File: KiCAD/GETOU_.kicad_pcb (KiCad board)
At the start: 2 copper layers, 106.5 x 58 mm, 25 parts, among them U1 XIAO-RP2040-DIP

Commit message: Add and modify files
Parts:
- moved U1 12.8 mm to (191.0, 93.5)
- moved S12 11.7 mm to (170.5, 110.5)
- moved S11 11.2 mm to (170.8, 92.0)
- moved S9 10.8 mm to (152.3, 110.5)
- moved S10 10.5 mm to (170.8, 73.4)
- moved S8 9.95 mm to (152.3, 92.0)
- moved S6 9.55 mm to (133.5, 110.5)
- moved S7 9.18 mm to (152.3, 73.4)
- moved S3 8.63 mm to (115.0, 110.5)
- moved D10 8.57 mm to (96.0, 106.7)
- moved D5 8.57 mm to (96.0, 88.9)
- moved D1 8.57 mm to (96.0, 74.7)
- moved D11 8.57 mm to (96.0, 110.2)
- moved D12 8.57 mm to (96.0, 113.8)
- moved D2 8.57 mm to (96.0, 78.2)
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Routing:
- net Net-(D11-A): track 96.5 -> 114.3 mm
- net row0: track 120.5 -> 130.7 mm
- net col3: track 106.2 -> 114.2 mm
- net col1: track 124.5 -> 131.3 mm
- net Net-(D4-A): track 42.4 -> 49.0 mm
- net Net-(D6-A): track 42.9 -> 49.0 mm
- net col2: track 117.8 -> 123.4 mm
- net col0: track 149.0 -> 143.5 mm
- net row2: track 73.6 -> 78.0 mm
- net row1: track 98.8 -> 103.2 mm
- net Net-(D8-A): track 53.7 -> 56.5 mm
- net Net-(D9-A): track 67.8 -> 70.4 mm, vias 1 -> 0
- net Net-(D3-A): track 42.4 -> 44.9 mm
- net Net-(D2-A): track 30.4 -> 28.0 mm
- net Net-(D12-A): track 52.5 -> 54.7 mm
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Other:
- board size 106.5 x 58 mm -> 111.5 x 62 mm

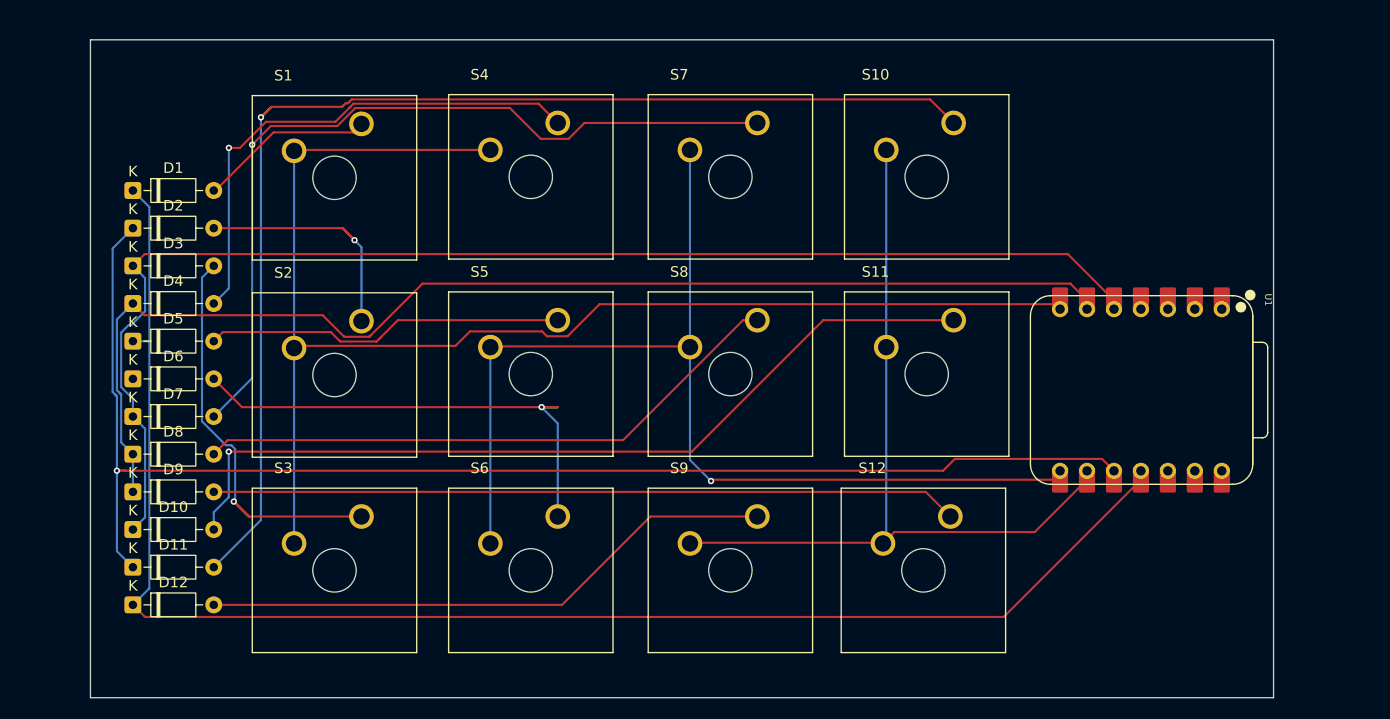
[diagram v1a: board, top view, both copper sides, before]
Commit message: Deleted files:     Firmware/qmk/keyboards/getou_/config.h     Firmware/qmk/keyboards/getou_/rules.mk     Fusion/PCB.stl
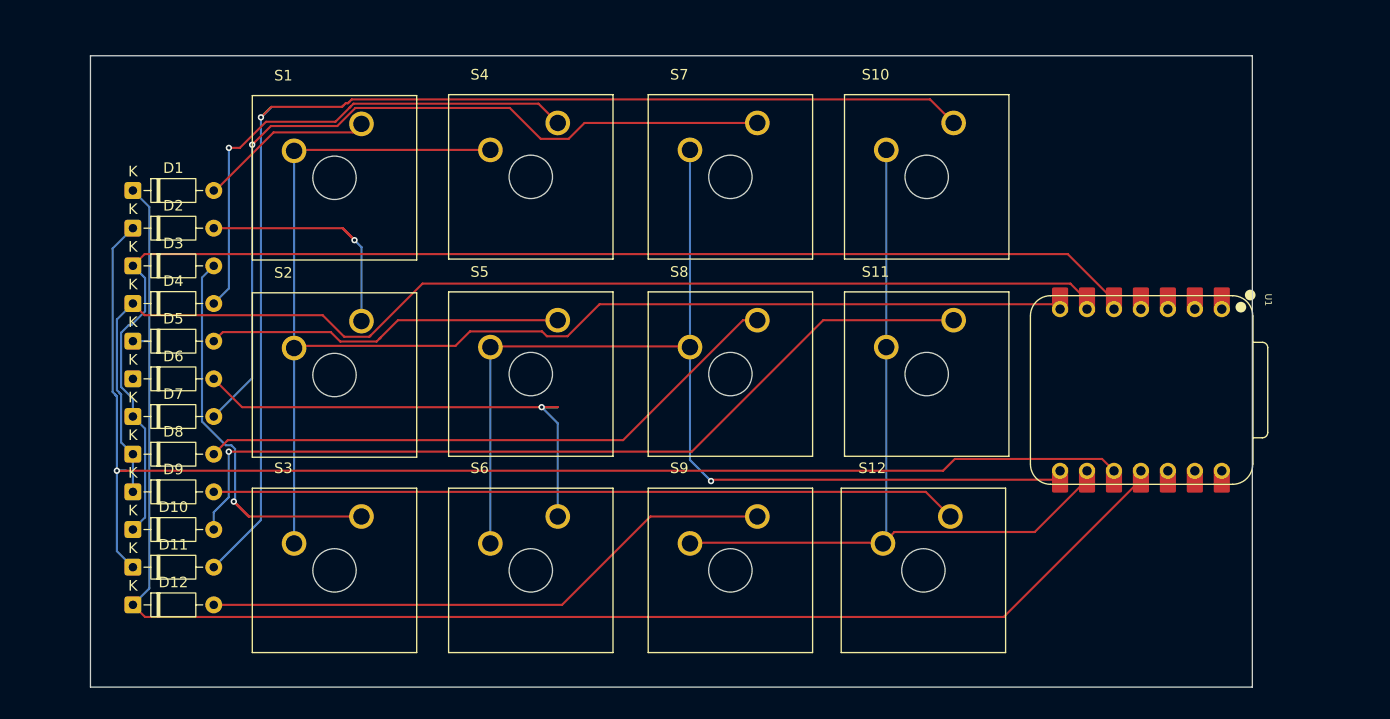
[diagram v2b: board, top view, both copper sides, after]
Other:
- board size 111.5 x 62 mm -> 109.5 x 59.5 mm
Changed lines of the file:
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@@
 		)
 	)
-	(gr_line
-		(start 203.5 93)
-		(end 203.5 60.5)
+	(gr_rect
+		(start 92 62)
+		(end 201.5 121.5)
 		(stroke
 			(width 0.05)
 			(type default)
 		)
-		(layer "Edge.Cuts")
-	)
-	(gr_line
-		(start 203.5 60.5)
-		(end 92 60.5)
-		(stroke
-			(width 0.05)
-			(type default)
-		)
-		(layer "Edge.Cuts")
-	)
-	(gr_line
-		(start 92 60.5)
-		(end 92 122.5)
-		(stroke
-			(width 0.05)
-			(type default)
-		)
-		(layer "Edge.Cuts")
-	)
-	(gr_line
-		(start 203.5 122.5)
-		(end 203.5 93)
-		(stroke
-			(width 0.05)
-			(type default)
-		)
-		(layer "Edge.Cuts")
-	)
-	(gr_line
-		(start 92 122.5)
-		(end 203.5 122.5)
-		(stroke
-			(width 0.05)
-			(type default)
-		)
+		(fill no)
 		(layer "Edge.Cuts")
 	)
@@
 		(polygon
 			(pts
-				(xy 203.5 60.5) (xy 203.5 122.5) (xy 92 122.5) (xy 92 60.5)
+				(xy 201.5 62) (xy 201.5 121.5) (xy 92 121.5) (xy 92 62)
 			)
 		)

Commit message: Add stuff
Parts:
- moved U1 8.82 mm to (199.6, 91.6), turned to 0 degrees
- moved S10 7.14 mm to (177.8, 72.0)
- moved S11 7.07 mm to (177.8, 91.0)
- moved S12 7.02 mm to (177.5, 110.0)
- moved S7 6.84 mm to (159.0, 72.0)
- moved S8 6.76 mm to (159.0, 91.0)
- moved S9 6.71 mm to (159.0, 110.0)
- moved S1 6.61 mm to (121.3, 71.5)
- moved S4 6.35 mm to (139.6, 71.5)
- moved S2 6.10 mm to (121.0, 91.0)
- moved S5 6.08 mm to (139.5, 91.0)
- moved S3 6.02 mm to (121.0, 110.0)
- moved S6 6.02 mm to (139.5, 110.0)
- moved D1 5.18 mm to (97.7, 69.8)
- moved D10 5.18 mm to (97.7, 101.8)
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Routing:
- net col0: track 143.5 -> 0.00 mm
- net col1: track 131.3 -> 0.00 mm, vias 1 -> 0
- net row0: track 130.7 -> 0.00 mm
- net col2: track 123.4 -> 0.00 mm
- net Net-(D11-A): track 114.3 -> 0.00 mm, vias 1 -> 0
- net col3: track 114.2 -> 0.00 mm
- net row1: track 103.2 -> 0.00 mm, vias 1 -> 0
- net Net-(D10-A): track 81.4 -> 0.00 mm, vias 1 -> 0
- net Net-(D7-A): track 79.3 -> 0.00 mm, vias 1 -> 0
- net row2: track 78.0 -> 0.00 mm
- net Net-(D9-A): track 70.4 -> 0.00 mm
- net Net-(D8-A): track 56.5 -> 0.00 mm
- net Net-(D12-A): track 54.7 -> 0.00 mm
- net Net-(D6-A): track 49.0 -> 0.00 mm, vias 1 -> 0
- net Net-(D4-A): track 49.0 -> 0.00 mm, vias 1 -> 0
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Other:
- board outline removed

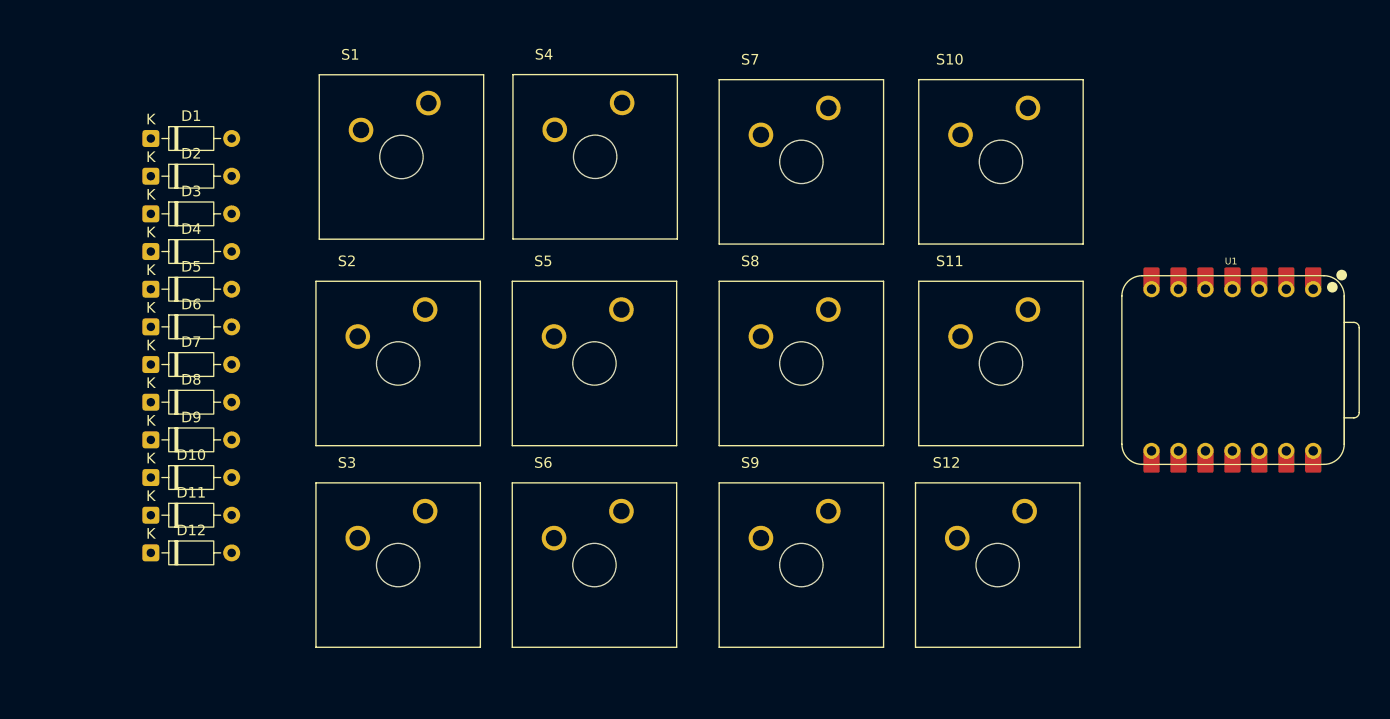
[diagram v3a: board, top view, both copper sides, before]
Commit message: Fix values in GETOU_ project files for improved accuracy
- Updated numerical values in GETOU_.kicad_prl to correct component specifications.
- Adjusted positions of global labels in GETOU_.kicad_sch for better alignment and clarity.
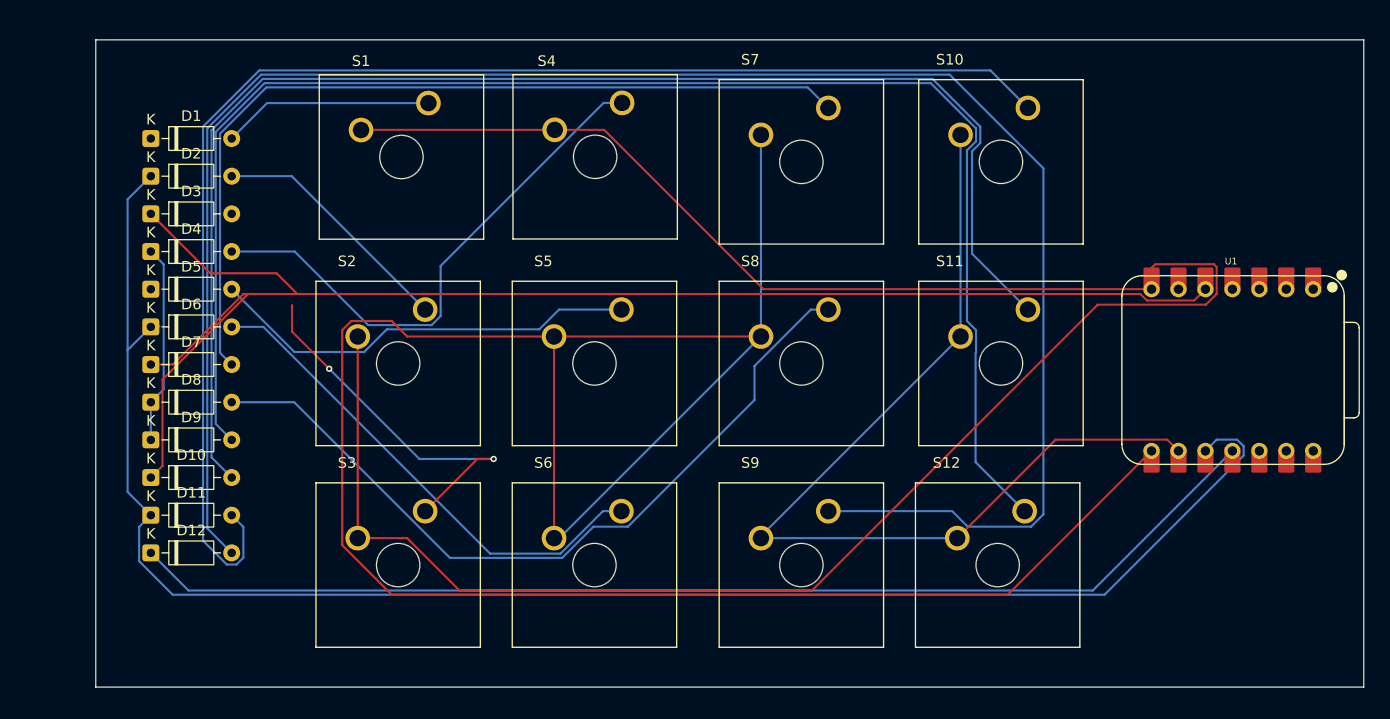
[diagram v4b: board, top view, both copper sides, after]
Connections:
- D6 pad 1: unconnected-(D6-K-Pad1) -> col1
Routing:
- net row1: track 0.00 -> 209.9 mm
- net row0: track 0.00 -> 205.2 mm
- net Net-(D12-A): track 0.00 -> 179.5 mm
- net col1: track 0.00 -> 159.4 mm
- net Net-(D9-A): track 0.00 -> 143.7 mm
- net col2: track 0.00 -> 143.5 mm
- net Net-(D11-A): track 0.00 -> 129.9 mm
- net Net-(D10-A): track 0.00 -> 129.6 mm
- net col0: track 0.00 -> 108.8 mm
- net row2: track 0.00 -> 89.4 mm
- net Net-(D7-A): track 0.00 -> 82.2 mm
- net Net-(D8-A): track 0.00 -> 73.9 mm
- net Net-(D4-A): track 0.00 -> 51.1 mm
- net Net-(D6-A): track 0.00 -> 47.2 mm
- net Net-(D5-A): track 0.00 -> 40.8 mm
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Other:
- board outline added: 119.5 x 61 mm

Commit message: Modify Files
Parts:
- moved S5 2.60 mm to (142.1, 90.6)
- moved S6 2.57 mm to (142.1, 110.0)
- moved S4 2.53 mm to (142.1, 71.1)
- moved U1 1.95 mm to (200.5, 89.9)
- moved S7 1.68 mm to (160.5, 71.2)
- moved S8 1.52 mm to (160.5, 90.6)
- moved S12 1.50 mm to (179.0, 110.0)
- moved S10 1.46 mm to (179.0, 71.1)
- moved S9 1.46 mm to (160.5, 110.0)
- moved S11 1.27 mm to (179.0, 90.6)
- moved S3 1.09 mm to (122.0, 110.4)
- moved S2 1.00 mm to (122.0, 91.0)
- moved S1 0.69 mm to (122.0, 71.6)
- moved D3 0.21 mm to (97.5, 76.8)
- moved D4 0.21 mm to (97.5, 80.3)
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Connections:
- D10 pad 1: col2 -> col1
- D11 pad 1: col1 -> col0
- D12 pad 1: col0 -> col2
- D4 pad 1: col3 -> col0
- D5 pad 1: col0 -> col1
- D6 pad 1: col1 -> col2
- D7 pad 1: col2 -> col0
- D8 pad 1: col3 -> col1
- D9 pad 1: col3 -> col2
- S10 pad 1: row2 -> row3
- S11 pad 1: row2 -> row3
- S12 pad 1: row2 -> row3
- S4 pad 1: row0 -> row1
- S7 pad 1: row1 -> row2
- S8 pad 1: row1 -> row2
- U1 pad 6: col3 -> row3
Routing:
- net row1: track 209.9 -> 38.9 mm
- net row0: track 205.2 -> 41.4 mm, vias 0 -> 2
- net col1: track 159.4 -> 0.00 mm
- net Net-(D11-A): track 129.9 -> 0.00 mm
- net row3: track 0.00 -> 106.0 mm
- net Net-(D12-A): track 179.5 -> 104.8 mm
- net Net-(D9-A): track 143.7 -> 88.9 mm
- net Net-(D6-A): track 47.2 -> 0.00 mm
- net Net-(D10-A): track 129.6 -> 91.6 mm
- net col0: track 108.8 -> 144.3 mm
- net Net-(D3-A): track 35.5 -> 0.00 mm, vias 2 -> 0
- net Net-(D8-A): track 73.9 -> 109.1 mm
- net col3: track 18.8 -> 0.00 mm
- net col2: track 143.5 -> 160.7 mm, vias 0 -> 1
- net Net-(D7-A): track 82.2 -> 68.6 mm
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
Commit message: Modifiy Files
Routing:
- net col1: track 0.00 -> 134.4 mm, vias 0 -> 1
- net Net-(D8-A): track 109.1 -> 216.7 mm
- net Net-(D11-A): track 0.00 -> 106.5 mm, vias 0 -> 1
- net Net-(D12-A): track 104.8 -> 207.5 mm
- net Net-(D10-A): track 91.6 -> 180.2 mm
- net Net-(D9-A): track 88.9 -> 174.9 mm
- net row0: track 41.4 -> 122.7 mm
- net row3: track 106.0 -> 171.7 mm
- net row1: track 38.9 -> 99.0 mm
- net Net-(D6-A): track 0.00 -> 52.1 mm, vias 0 -> 2
- net col2: track 160.7 -> 206.7 mm
- net row2: track 77.9 -> 121.4 mm
- net Net-(D3-A): track 0.00 -> 42.0 mm, vias 0 -> 1
- net Net-(D7-A): track 68.6 -> 103.3 mm
- net col0: track 144.3 -> 176.5 mm
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
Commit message: Modify Files
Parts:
- moved D12 7.27 mm to (98.0, 116.0)
- moved D11 6.32 mm to (98.0, 111.5)
- moved D10 5.37 mm to (98.0, 107.0)
- moved D9 4.38 mm to (98.0, 102.5)
- moved D8 3.59 mm to (98.0, 98.1)
- moved S5 2.91 mm to (139.3, 91.5)
- moved S4 2.90 mm to (139.3, 72.0)
- moved D1 2.88 mm to (98.2, 66.9)
- moved S6 2.76 mm to (139.3, 110.0)
- moved D7 2.65 mm to (98.0, 93.6)
- moved S8 2.63 mm to (158.0, 91.5)
- moved S7 2.60 mm to (158.0, 72.0)
- moved S9 2.46 mm to (158.0, 110.0)
- moved D2 2.35 mm to (98.2, 71.0)
- moved D6 1.72 mm to (98.0, 89.1)
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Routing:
- net row0: track 122.7 -> 293.5 mm, vias 2 -> 1
- net col1: track 134.4 -> 275.1 mm, vias 1 -> 0
- net col0: track 176.5 -> 308.2 mm
- net row1: track 99.0 -> 223.3 mm
- net Net-(D8-A): track 216.7 -> 103.0 mm
- net Net-(D11-A): track 106.5 -> 207.2 mm
- net Net-(D9-A): track 174.9 -> 79.2 mm
- net row3: track 171.7 -> 86.6 mm
- net Net-(D12-A): track 207.5 -> 126.3 mm
- net col2: track 206.7 -> 282.0 mm, vias 1 -> 0
- net Net-(D6-A): track 52.1 -> 105.8 mm, vias 2 -> 0
- net Net-(D2-A): track 28.4 -> 64.4 mm, vias 2 -> 0
- net Net-(D4-A): track 70.7 -> 97.8 mm
- net Net-(D7-A): track 103.3 -> 124.1 mm, vias 0 -> 1
- net Net-(D3-A): track 42.0 -> 61.3 mm, vias 1 -> 0
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
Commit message: Modify Files
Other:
- board text added: "getou_ Made by Kaihang(gnahiak2)"
